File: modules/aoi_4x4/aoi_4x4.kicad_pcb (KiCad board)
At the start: 2 copper layers, 29.2 x 33 mm, 37 parts, among them J1 Conn_02x12_Odd_Even, Q1 2N3906, Q10 2N3906, Q11 2N3906, Q12 2N3906, Q13 2N3906, Q14 2N3906, Q15 2N3906, Q16 2N3906, Q17 2N3906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

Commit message: Started working towards real modules. Modules with PCIe connectors.
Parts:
- J1: value Conn_02x12_Odd_Even -> Conn_02x18_Row_Letter_First; footprint Connector_PinHeader_2.54mm:PinHeader_2x12_P2.54mm_Horizontal -> Connector_PCBEdge:BUS_PCIexpress_x1
- moved J1 17.5 mm to (149.7, 64.1), turned to 90 degrees

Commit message: Started PCIe connector-based module design.
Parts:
- J1: footprint Connector_PCBEdge:BUS_PCIexpress_x1 -> Connector_PCBEdge:BUS_PCIexpress_x4
- moved J1 12.7 mm to (149.4, 76.8)
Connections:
- J1 pad A1: (no net) -> unconnected-(J1-Pin_a1-PadA1)
- J1 pad A10: (no net) -> unconnected-(J1-Pin_a10-PadA10)
- J1 pad A11: (no net) -> unconnected-(J1-Pin_a11-PadA11)
- J1 pad A12: (no net) -> VCC
- J1 pad A13: (no net) -> /V_~{OUT}
- J1 pad A14: (no net) -> /~{OUT}
- J1 pad A15: (no net) -> /IN_A1
- J1 pad A16: (no net) -> /IN_A3
- J1 pad A17: (no net) -> /IN_B1
- J1 pad A18: (no net) -> /IN_B3
- J1 pad A2: (no net) -> unconnected-(J1-Pin_a2-PadA2)
- J1 pad A3: (no net) -> unconnected-(J1-Pin_a3-PadA3)
- J1 pad A4: (no net) -> unconnected-(J1-Pin_a4-PadA4)
- J1 pad A5: (no net) -> VCC
- J1 pad A6: (no net) -> unconnected-(J1-Pin_a6-PadA6)
- J1 pad A7: (no net) -> unconnected-(J1-Pin_a7-PadA7)
- J1 pad A8: (no net) -> unconnected-(J1-Pin_a8-PadA8)
- J1 pad A9: (no net) -> unconnected-(J1-Pin_a9-PadA9)
- J1 pad B1: (no net) -> unconnected-(J1-Pin_b1-PadB1)
- J1 pad B10: (no net) -> unconnected-(J1-Pin_b10-PadB10)
- J1 pad B11: (no net) -> unconnected-(J1-Pin_b11-PadB11)
- J1 pad B12: (no net) -> VCC
- J1 pad B13: (no net) -> /V_OUT
- J1 pad B14: (no net) -> /OUT
- J1 pad B15: (no net) -> /IN_A2
- J1 pad B16: (no net) -> /IN_A4
- J1 pad B17: (no net) -> /IN_B2
- J1 pad B18: (no net) -> /IN_B4
- J1 pad B2: (no net) -> unconnected-(J1-Pin_b2-PadB2)
- J1 pad B3: (no net) -> unconnected-(J1-Pin_b3-PadB3)
- J1 pad B4: (no net) -> unconnected-(J1-Pin_b4-PadB4)
- J1 pad B5: (no net) -> 0
- J1 pad B6: (no net) -> unconnected-(J1-Pin_b6-PadB6)
- J1 pad B7: (no net) -> unconnected-(J1-Pin_b7-PadB7)
- J1 pad B8: (no net) -> unconnected-(J1-Pin_b8-PadB8)
- J1 pad B9: (no net) -> unconnected-(J1-Pin_b9-PadB9)
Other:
- board size 29.2 x 33 mm -> 21.3 x 34.3 mm

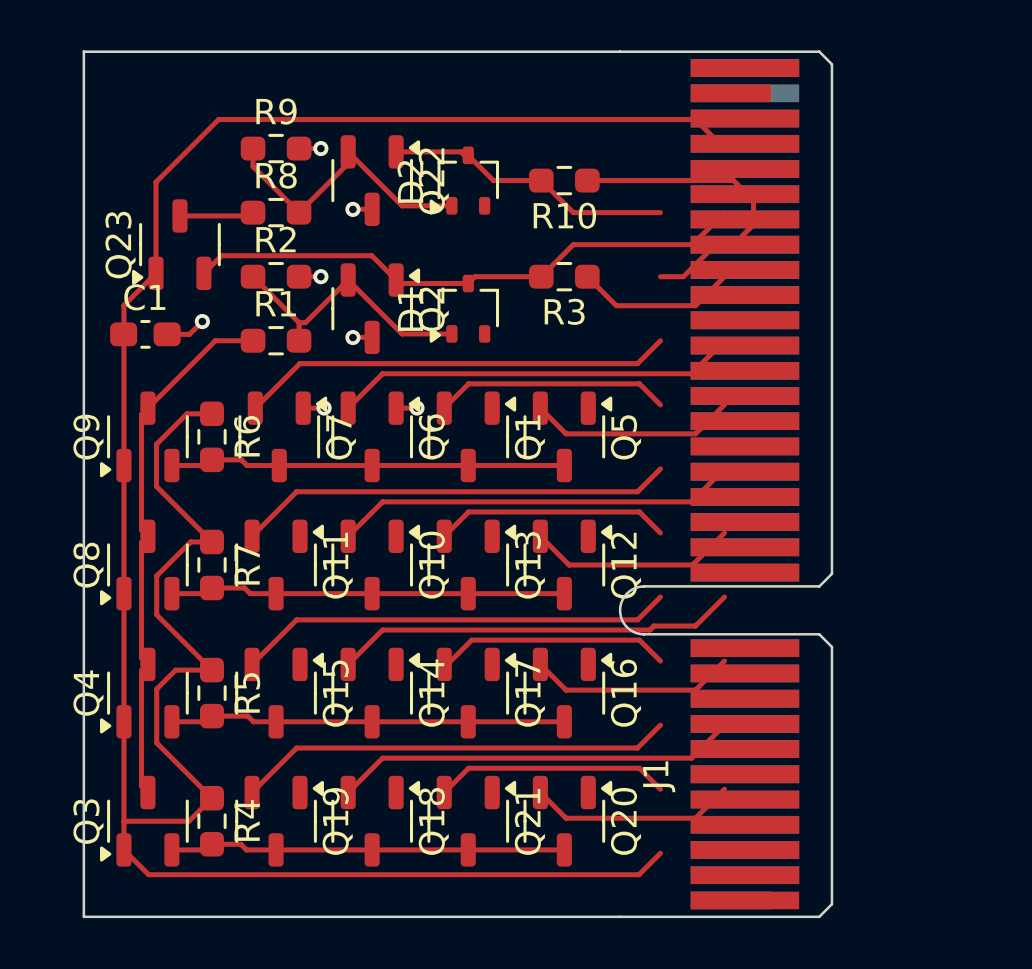
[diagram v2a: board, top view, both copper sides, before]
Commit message: More work on AOI PCB. Fully routed, but not clean yet.
Also needs bypass caps.
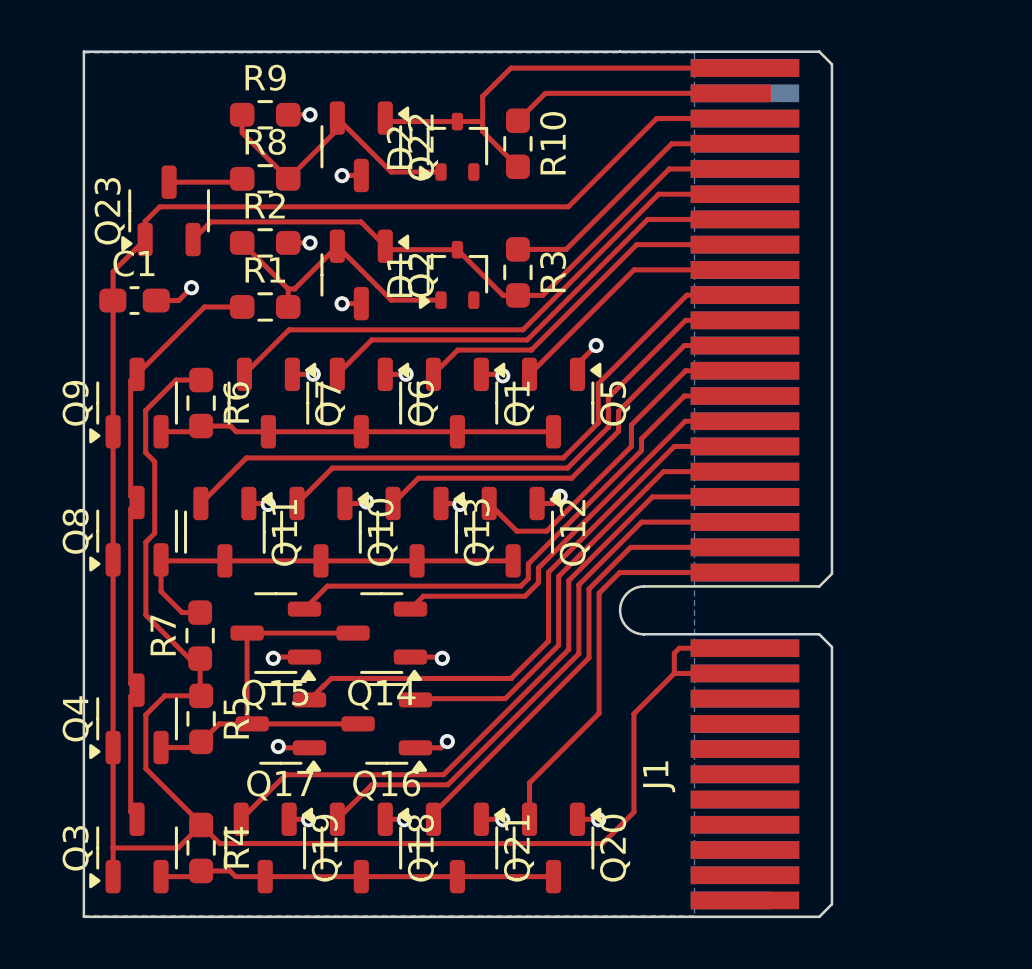
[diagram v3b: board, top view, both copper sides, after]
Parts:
- moved Q17 7.53 mm to (131.0, 69.8), turned to 180 degrees
- moved Q16 7.14 mm to (135.2, 69.8), turned to 180 degrees
- moved R7 2.84 mm to (127.8, 66.3), turned to 90 degrees
- moved Q10 2.41 mm to (132.6, 62.2)
- moved Q11 2.41 mm to (128.8, 62.2)
- moved Q12 2.41 mm to (140.2, 62.2)
- moved Q13 2.41 mm to (136.4, 62.2)
- moved Q14 2.41 mm to (135.0, 66.2), turned to 180 degrees
- moved Q15 2.38 mm to (130.8, 66.2), turned to 180 degrees
- moved R10 2.35 mm to (140.4, 46.8), turned to -90 degrees
- moved R3 1.85 mm to (140.4, 51.9), turned to -90 degrees
- moved D1 1.41 mm to (138.0, 52.0)
- moved Q1 1.41 mm to (138.0, 57.1)
- moved Q2 1.41 mm to (134.2, 52.0)
- moved Q5 1.41 mm to (141.8, 57.1)
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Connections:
- J1 pad A10: unconnected-(J1-Pin_a10-PadA10) -> 0
- J1 pad A11: unconnected-(J1-Pin_a11-PadA11) -> 0
- J1 pad A12: VCC -> 0
- J1 pad A13: /V_~{OUT} -> 0
- J1 pad A14: /~{OUT} -> 0
- J1 pad A15: /IN_A1 -> 0
- J1 pad A16: /IN_A3 -> 0
- J1 pad A17: /IN_B1 -> 0
- J1 pad A18: /IN_B3 -> 0
- J1 pad A19: /IN_C1 -> 0
- J1 pad A20: /IN_C3 -> 0
- J1 pad A21: /IN_D1 -> 0
- J1 pad A22: /IN_D3 -> 0
- J1 pad A23: unconnected-(J1-Pin_a23-PadA23) -> 0
- J1 pad A24: unconnected-(J1-Pin_a24-PadA24) -> 0
- J1 pad A25: unconnected-(J1-Pin_a25-PadA25) -> 0
- J1 pad A26: unconnected-(J1-Pin_a26-PadA26) -> 0
- J1 pad A27: unconnected-(J1-Pin_a27-PadA27) -> 0
- J1 pad A28: unconnected-(J1-Pin_a28-PadA28) -> 0
- J1 pad A29: unconnected-(J1-Pin_a29-PadA29) -> 0
- J1 pad A30: unconnected-(J1-Pin_a30-PadA30) -> 0
- J1 pad A31: unconnected-(J1-Pin_a31-PadA31) -> 0
- J1 pad A32: unconnected-(J1-Pin_a32-PadA32) -> 0
- J1 pad A5: VCC -> unconnected-(J1-Pin_a5-PadA5)
- J1 pad B10: unconnected-(J1-Pin_b10-PadB10) -> VCC
- J1 pad B11: unconnected-(J1-Pin_b11-PadB11) -> VCC
- J1 pad B12: VCC -> /IN_D3
- J1 pad B13: /V_OUT -> /IN_D4
- J1 pad B14: /OUT -> /IN_D1
- J1 pad B15: /IN_A2 -> /IN_D2
- J1 pad B16: /IN_A4 -> /IN_C3
- J1 pad B17: /IN_B2 -> /IN_C4
- J1 pad B18: /IN_B4 -> /IN_C1
- J1 pad B20: /IN_C4 -> /IN_B3
- J1 pad B21: /IN_D2 -> /IN_B4
- J1 pad B22: /IN_D4 -> /IN_B1
- J1 pad B23: unconnected-(J1-Pin_b23-PadB23) -> /IN_B2
- J1 pad B24: unconnected-(J1-Pin_b24-PadB24) -> /IN_A3
- J1 pad B25: unconnected-(J1-Pin_b25-PadB25) -> /IN_A4
- J1 pad B26: unconnected-(J1-Pin_b26-PadB26) -> /IN_A1
- J1 pad B27: unconnected-(J1-Pin_b27-PadB27) -> /IN_A2
- J1 pad B28: unconnected-(J1-Pin_b28-PadB28) -> /~{OUT}
- J1 pad B29: unconnected-(J1-Pin_b29-PadB29) -> /V_~{OUT}
- J1 pad B30: unconnected-(J1-Pin_b30-PadB30) -> VCC
- J1 pad B31: unconnected-(J1-Pin_b31-PadB31) -> /V_OUT
- J1 pad B32: unconnected-(J1-Pin_b32-PadB32) -> /OUT
- J1 pad B5: 0 -> unconnected-(J1-Pin_b5-PadB5)
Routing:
- net 0: track 6.53 -> 20.7 mm, vias 7 -> 21
- net /IN_C4: track 9.37 -> 23.0 mm
- net /IN_C3: track 8.20 -> 18.4 mm
- net VCC: track 99.6 -> 109.7 mm
- net /IN_D2: track 17.3 -> 26.9 mm
- net /IN_D4: track 9.31 -> 18.6 mm
- net /IN_B2: track 17.3 -> 25.9 mm
- net /IN_D3: track 8.20 -> 16.2 mm
- net /IN_B4: track 9.31 -> 17.0 mm
- net /OUT: track 11.5 -> 18.2 mm
- net /IN_D1: track 16.0 -> 22.6 mm
- net /IN_A2: track 17.2 -> 22.8 mm
- net /IN_B3: track 8.30 -> 13.7 mm
- net /IN_B1: track 16.0 -> 21.5 mm
- net /IN_A4: track 9.31 -> 14.5 mm
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- added copper zone on B.Cu, net 0

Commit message: More flushed out library and it's use. PCB is also much nicer.
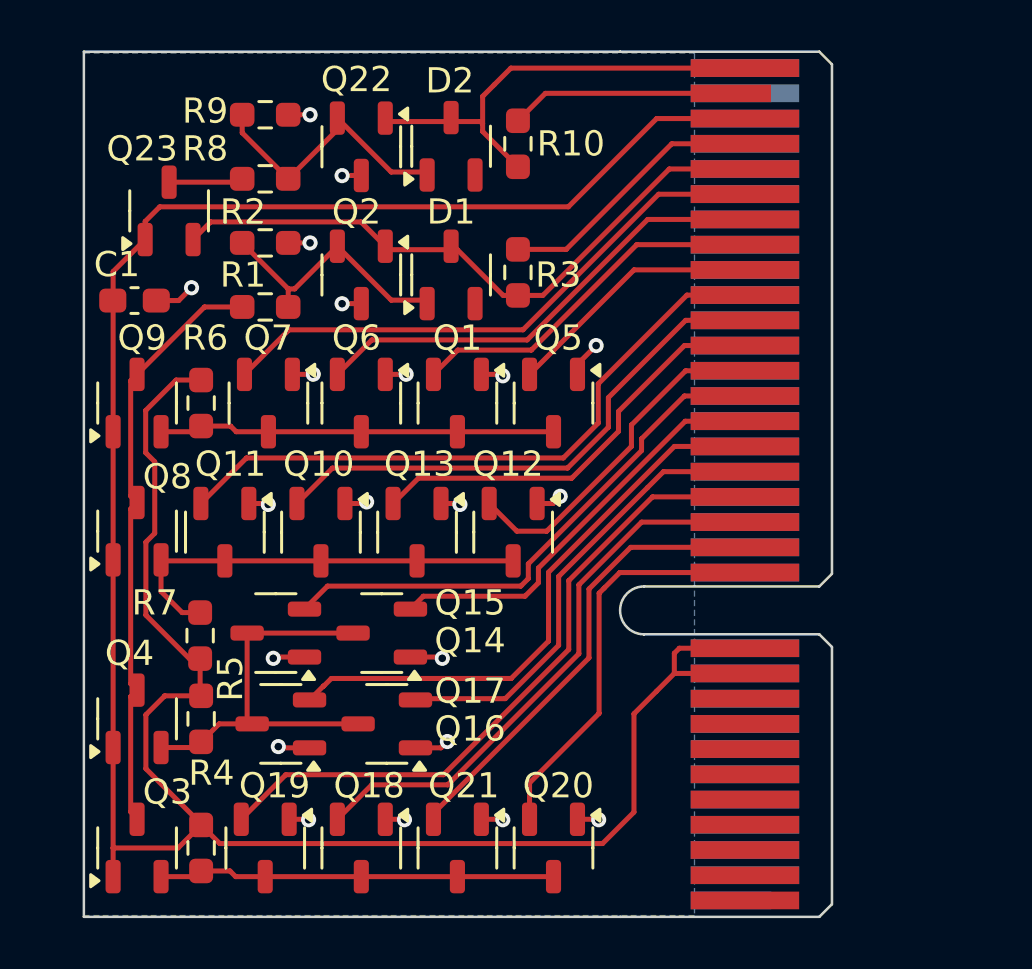
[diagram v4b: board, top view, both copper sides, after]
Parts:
- D1, D2: value BAT54W -> BAT54LT1G; footprint Package_TO_SOT_SMD:SOT-323_SC-70 -> Package_TO_SOT_SMD:SOT-23-3
- J1: footprint Connector_PCBEdge:BUS_PCIexpress_x4 -> tcomp:BUS_PCIexpress_x4
- moved D2 0.25 mm to (137.8, 46.9)
- moved D1 0.25 mm to (137.8, 52.0)
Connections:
- net 0 renamed GND
- net Net-(D1-A) renamed /X2
- net Net-(D2-A) renamed /Y2
- net Net-(Q1-E) renamed /A
- net Net-(Q10-E) renamed /B
- net Net-(Q14-E) renamed /C
- net Net-(Q18-E) renamed /D
- net Net-(Q23-E) renamed /Y
- net Net-(Q3-E) renamed /X
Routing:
- net /Y2: track 11.5 -> 11.0 mm
